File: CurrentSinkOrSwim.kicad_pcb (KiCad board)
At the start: 2 copper layers, 41.7 x 47.8 mm, 23 parts, among them P1 CONN_01X01, P101 CONN_01X02, P102 CONN_01X03, P103 CONN_01X02, Q401 BUK9575, U201 LMV358, U301 LM2931D-R

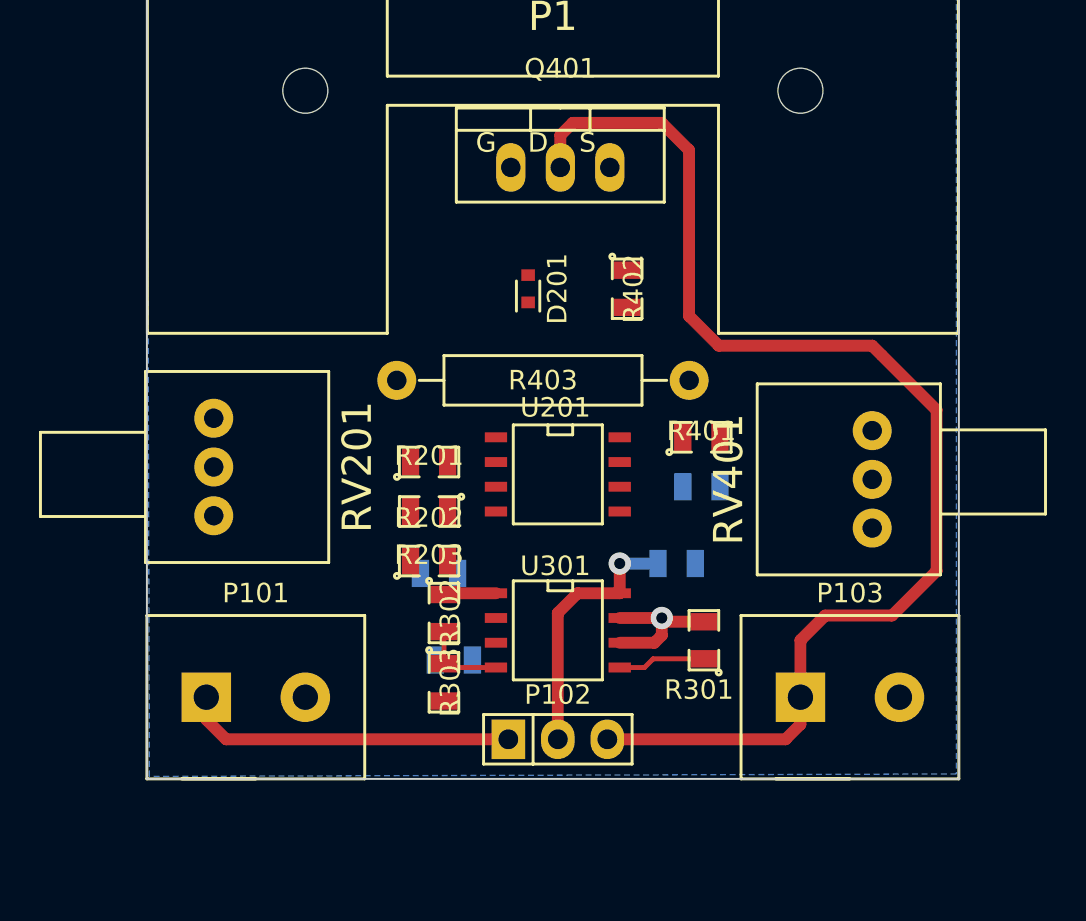
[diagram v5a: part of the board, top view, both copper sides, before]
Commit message: Moved pots/terms and routed traces to all components
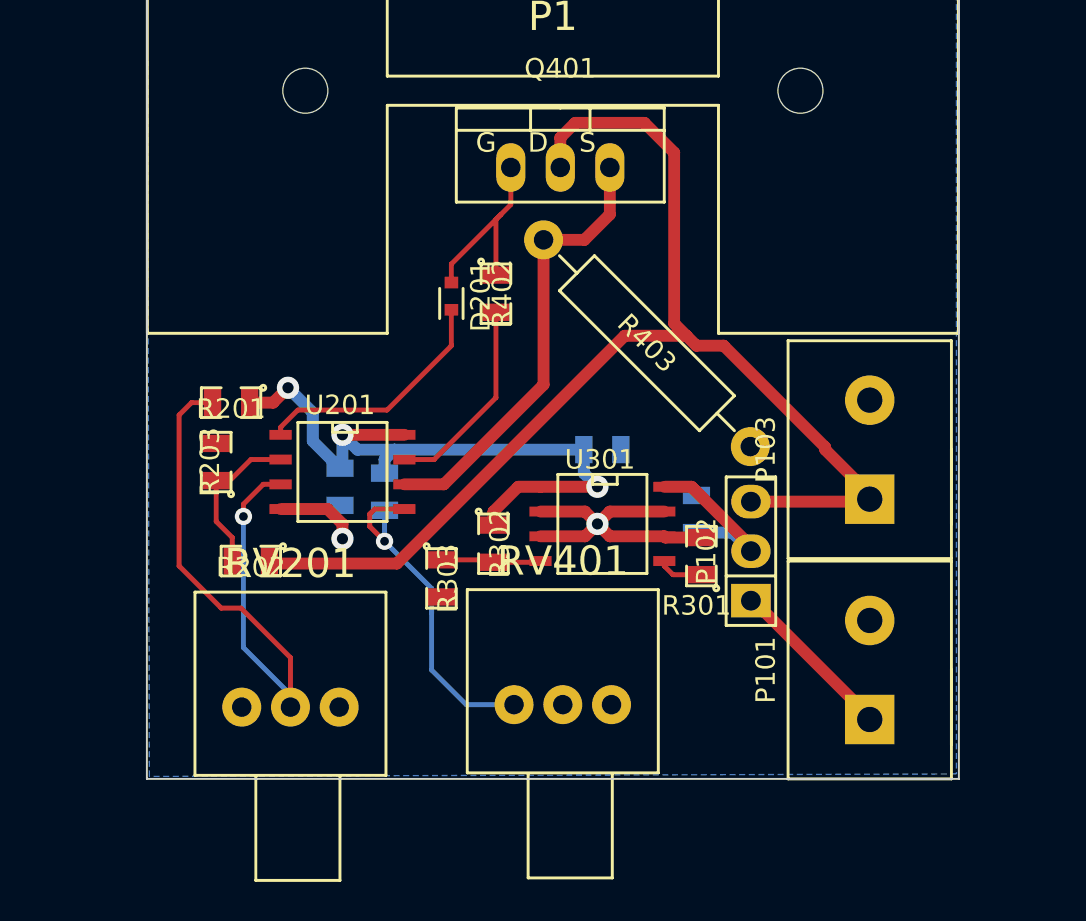
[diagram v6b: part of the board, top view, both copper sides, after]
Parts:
- removed C401: C, SMD_Packages:SMD-0805
- R401: moved to B.Cu
- moved P101 31.5 mm to (143.3, 78.0), turned to 90 degrees
- moved RV401 19.6 mm to (127.5, 79.8), turned to 0 degrees
- moved R401 16.5 mm to (118.4, 68.8), turned to 270 degrees
- moved P102 13.8 mm to (137.2, 71.9), turned to 90 degrees
- moved RV201 12.9 mm to (113.5, 79.9), turned to 0 degrees
- moved P103 12.7 mm to (143.3, 66.7), turned to 90 degrees
- moved R203 12.0 mm to (109.7, 67.3), turned to 90 degrees
- moved U201 11.0 mm to (116.2, 67.8)
- moved C201 10.6 mm to (116.1, 68.6), turned to 270 degrees
- moved R201 10.6 mm to (110.5, 64.3), turned to 180 degrees
- moved C302 10.5 mm to (129.5, 66.7), turned to 0 degrees
- moved R202 9.49 mm to (111.5, 72.4)
- moved R402 6.74 mm to (124.1, 58.7)
- moved U301 5.92 mm to (129.5, 70.5)
- moved R403 5.66 mm to (131.8, 61.2), turned to 315 degrees
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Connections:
- R203 pad 2: /Voltage Control/Current_Sink- -> GND
- RV201 pad 3: /Voltage Control/Current_Sink- -> GND
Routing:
- net Net-(R201-Pad2): track 0.00 -> 33.7 mm, vias 0 -> 1
- net 2.7V: track 2.69 -> 35.3 mm, vias 0 -> 3
- net Net-(Q401-PadS): track 0.00 -> 23.0 mm
- net Net-(R401-Pad2): track 0.00 -> 17.9 mm, vias 0 -> 1
- net Net-(D201-Pad2): track 0.00 -> 12.7 mm
- net GND: track 7.60 -> 20.2 mm, vias 1 -> 2
- net Net-(R402-Pad2): track 0.00 -> 10.4 mm
- net /Current Control/FET_Gate: track 0.00 -> 10.4 mm
- net Net-(P101-Pad1): track 17.1 -> 8.70 mm
- net Net-(R202-Pad2): track 0.00 -> 8.31 mm
- net /Power Regulation/Vin: track 13.6 -> 10.0 mm, vias 1 -> 0
- net Net-(R301-Pad1): track 4.50 -> 2.34 mm
- net Net-(R302-Pad2): track 4.40 -> 5.16 mm

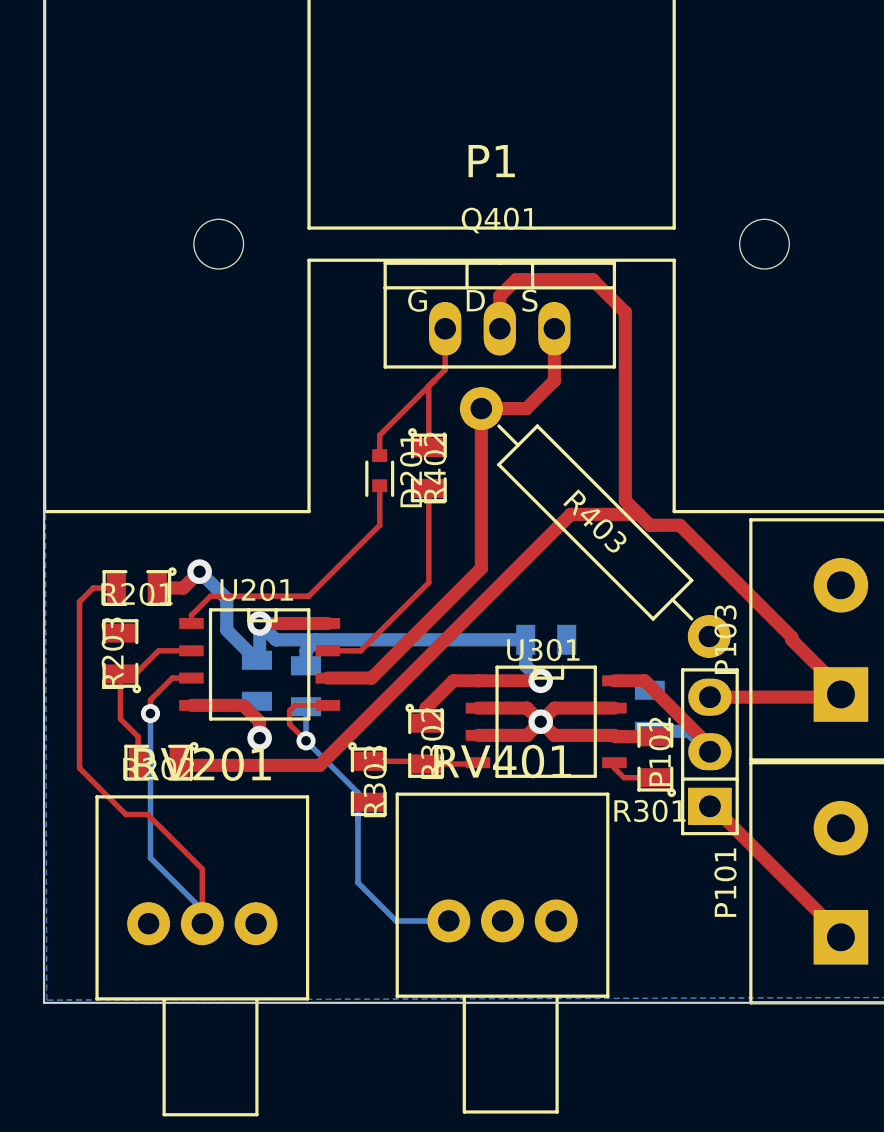
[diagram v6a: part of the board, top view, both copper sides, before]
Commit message: Ground fill and DRC
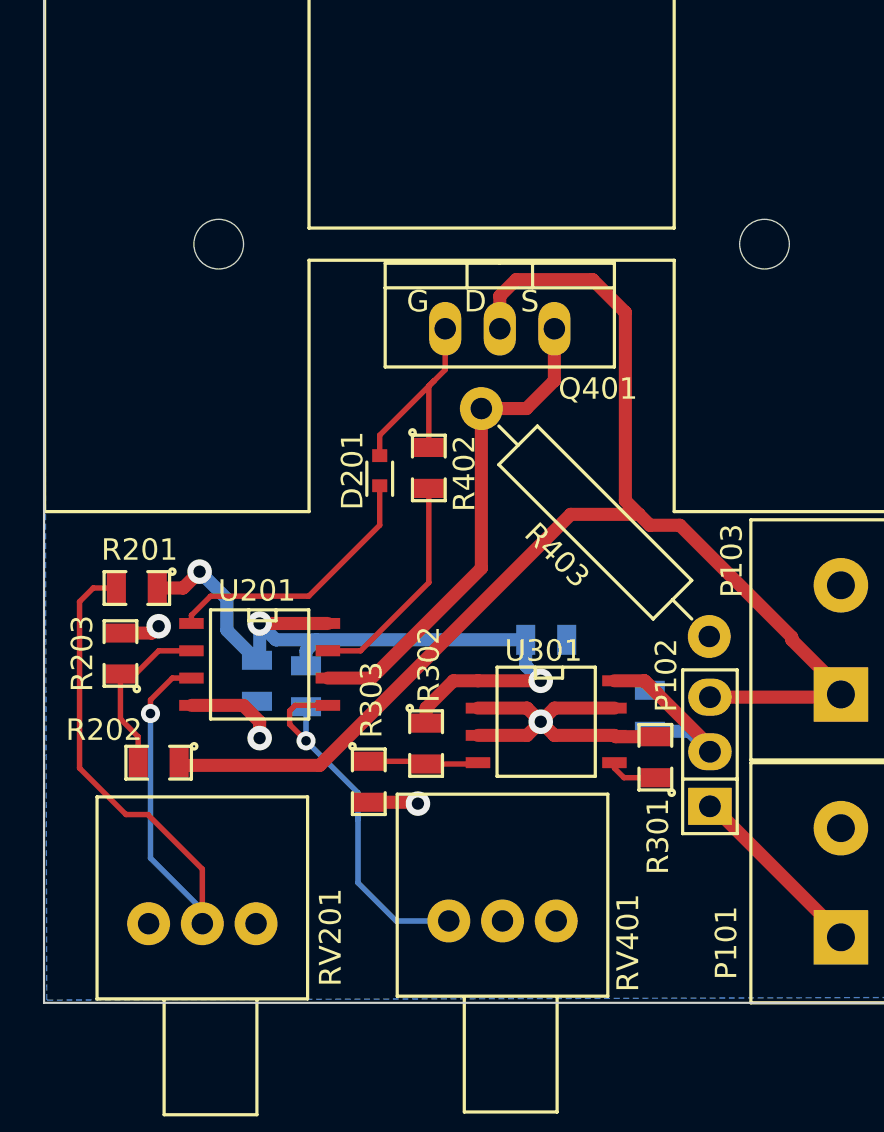
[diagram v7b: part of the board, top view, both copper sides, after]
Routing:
- net GND: track 20.2 -> 24.5 mm, vias 2 -> 4

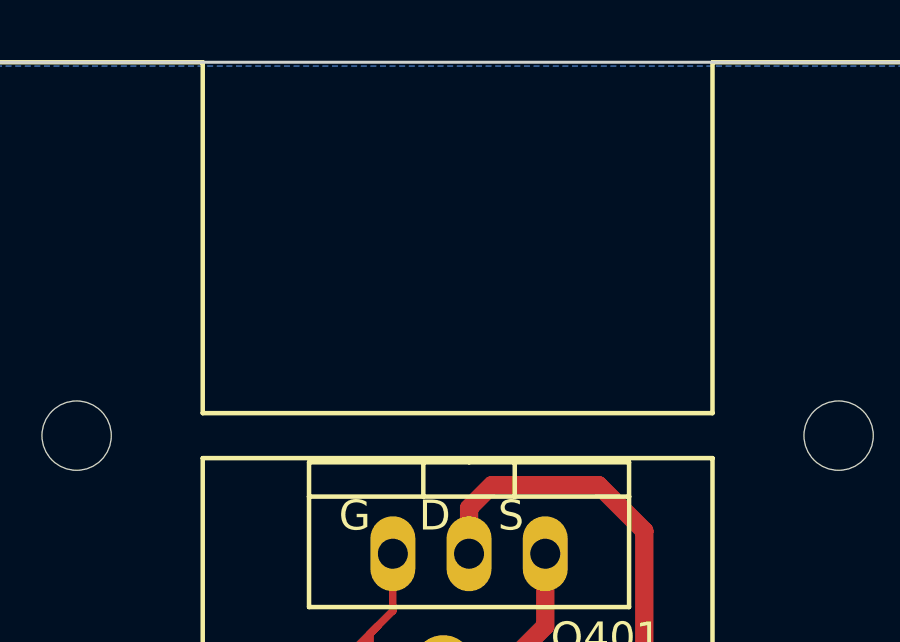
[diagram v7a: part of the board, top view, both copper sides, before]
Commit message: Added graphic and text above heatsink
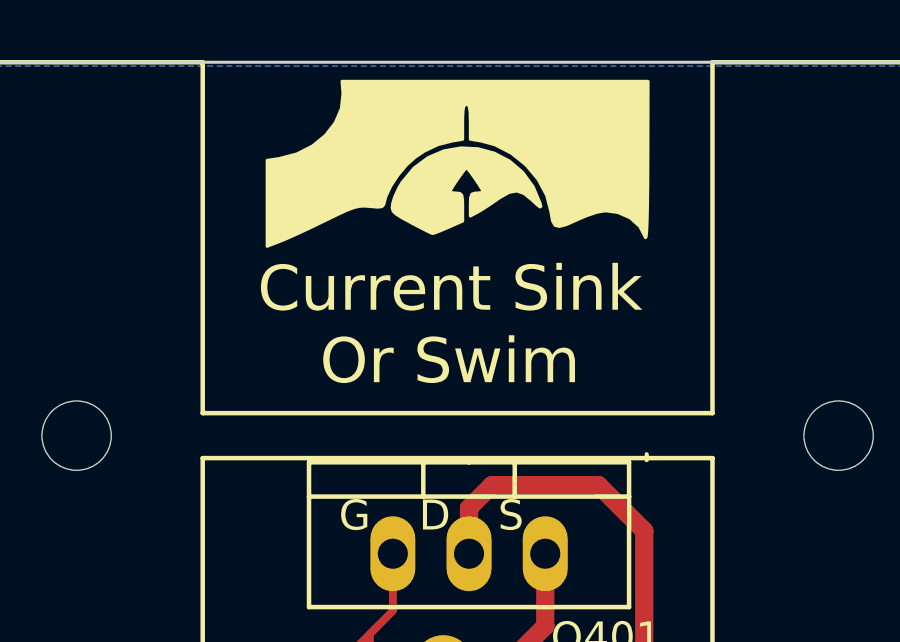
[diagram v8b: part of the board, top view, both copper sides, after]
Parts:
- added G***: LOGO, Current:CSOS, F.Cu at (127.0, 42.8)
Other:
- board text added: "Current Sink Or Swim"
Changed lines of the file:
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@@
 (kicad_pcb (version 4) (host pcbnew 0.201502010101+5397~21~ubuntu14.04.1-product)
   (general
-    (links 42)
+    (links 0)
     (no_connects 0)
-    (area 105.817599 35.434199 151.517134 89.152801)
+    (area 106.121999 35.763999 147.878001 83.616001)
     (thickness 1.6)
-    (drawings 4)
+    (drawings 5)
     (tracks 132)
     (zones 0)
-    (modules 22)
+    (modules 23)
     (nets 17)
   )
@@
     (34 B.Paste user)
     (35 F.Paste user)
-    (36 B.SilkS user hide)
+    (36 B.SilkS user)
     (37 F.SilkS user)
-    (38 B.Mask user hide)
+    (38 B.Mask user)
     (39 F.Mask user)
-    (40 Dwgs.User user hide)
+    (40 Dwgs.User user)
     (41 Cmts.User user)
-    (42 Eco1.User user hide)
-    (43 Eco2.User user hide)
+    (42 Eco1.User user)
+    (43 Eco2.User user)
     (44 Edge.Cuts user)
     (45 Margin user)
@@
     (pad_to_mask_clearance 0)
     (aux_axis_origin 0 0)
-    (visible_elements FFFF867F)
+    (visible_elements FFFFD7FF)
     (pcbplotparams
       (layerselection 0x00030_80000001)
@@
     (pad "" np_thru_hole oval (at -5.1 -3.3) (size 2 2.2) (drill oval 2 2.2) (layers *.Cu *.Mask F.SilkS))
   )
+  (module Current:CSOS (layer F.Cu)
+    (at 127 42.799)
+    (fp_text reference G*** (at 0 0) (layer F.SilkS) hide
+      (effects (font (thickness 0.3)))
+    )
+    (fp_text value LOGO (at 0.75 0) (layer F.SilkS) hide
+      (effects (font (thickness 0.3)))
+    )
+    (fp_poly (pts (xy 6.332589 6.248175) (xy 6.321406 6.2865) (xy 6.290503 6.297136) (xy 6.278701 6.180666)
+      (xy 6.292007 6.060471) (xy 6.321406 6.074833) (xy 6.332589 6.248175) (xy 6.332589 6.248175)) (layer F.SilkS) (width 0.1))
+    (fp_poly (pts (xy 6.35 -6.35) (xy 6.342364 -3.6195) (xy 6.338041 -2.844779) (xy 6.32992 -2.205589)
+      (xy 6.318217 -1.708474) (xy 6.30315 -1.359975) (xy 6.284937 -1.166635) (xy 6.263794 -1.134996)
+      (xy 6.260074 -1.14565) (xy 6.070103 -1.511787) (xy 5.754746 -1.796131) (xy 5.347069 -1.97661)
+      (xy 4.932164 -2.032) (xy 4.658011 -1.988116) (xy 4.293298 -1.867165) (xy 3.987667 -1.733968)
+      (xy 3.631328 -1.575223) (xy 3.393129 -1.511035) (xy 3.245805 -1.549173) (xy 3.162094 -1.697404)
+      (xy 3.114734 -1.963497) (xy 3.112456 -1.983355) (xy 2.968407 -2.545754) (xy 2.682376 -3.079807)
+      (xy 2.28171 -3.557623) (xy 1.79376 -3.95131) (xy 1.245874 -4.232976) (xy 0.783166 -4.358849)
+      (xy 0.423333 -4.417551) (xy 0.423333 -5.002776) (xy 0.415702 -5.322469) (xy 0.388292 -5.504557)
+      (xy 0.334326 -5.580271) (xy 0.296333 -5.588) (xy 0.226956 -5.552838) (xy 0.187441 -5.426531)
+      (xy 0.17101 -5.177851) (xy 0.169333 -5.002776) (xy 0.169333 -4.417551) (xy -0.181877 -4.358215)
+      (xy -0.66885 -4.233561) (xy -1.117966 -4.016975) (xy -1.41718 -3.817206) (xy -1.70709 -3.556147)
+      (xy -1.990765 -3.216269) (xy -2.230436 -2.850985) (xy -2.388332 -2.51371) (xy -2.420075 -2.398898)
+      (xy -2.458164 -2.244349) (xy -2.523351 -2.169874) (xy -2.662911 -2.154507) (xy -2.920638 -2.176926)
+      (xy -3.110434 -2.190699) (xy -3.279871 -2.181082) (xy -3.463619 -2.137161) (xy -3.696349 -2.048025)
+      (xy -4.01273 -1.90276) (xy -4.414301 -1.706803) (xy -4.843446 -1.498766) (xy -5.261431 -1.302511)
+      (xy -5.6233 -1.138746) (xy -5.884097 -1.028183) (xy -5.9055 -1.019844) (xy -6.35 -0.849138)
+      (xy -6.35 -2.282048) (xy -6.35 -3.714958) (xy -5.947834 -3.77494) (xy -5.360352 -3.928988)
+      (xy -4.839039 -4.193979) (xy -4.404201 -4.548819) (xy -4.076142 -4.972412) (xy -3.875168 -5.443665)
+      (xy -3.821583 -5.941482) (xy -3.824215 -5.981109) (xy -3.853554 -6.35) (xy 1.248223 -6.35)
+      (xy 6.35 -6.35) (xy 6.35 -6.35)) (layer F.SilkS) (width 0.1))
+    (fp_poly (pts (xy 2.775091 -2.176038) (xy 2.742605 -2.16183) (xy 2.630231 -2.252313) (xy 2.482437 -2.391834)
+      (xy 2.21545 -2.607974) (xy 1.974172 -2.69267) (xy 1.717188 -2.646432) (xy 1.40308 -2.469766)
+      (xy 1.312062 -2.406203) (xy 1.041096 -2.21941) (xy 0.78807 -2.057083) (xy 0.656166 -1.980695)
+      (xy 0.423333 -1.858319) (xy 0.423333 -2.241493) (xy 0.43199 -2.477447) (xy 0.47463 -2.589566)
+      (xy 0.576255 -2.623109) (xy 0.635 -2.624667) (xy 0.794269 -2.641222) (xy 0.846666 -2.672912)
+      (xy 0.802955 -2.764636) (xy 0.694539 -2.937779) (xy 0.555494 -3.142902) (xy 0.419898 -3.330567)
+      (xy 0.321828 -3.451336) (xy 0.296333 -3.471334) (xy 0.23311 -3.407918) (xy 0.113766 -3.250628)
+      (xy -0.02762 -3.048903) (xy -0.156974 -2.852181) (xy -0.240217 -2.7099) (xy -0.254 -2.672912)
+      (xy -0.181368 -2.63661) (xy -0.042334 -2.624667) (xy 0.078788 -2.612616) (xy 0.141917 -2.548868)
+      (xy 0.165826 -2.392029) (xy 0.169333 -2.157933) (xy 0.169333 -1.691199) (xy -0.306869 -1.4806)
+      (xy -0.565549 -1.370487) (xy -0.758831 -1.296161) (xy -0.836036 -1.275016) (xy -0.92966 -1.314833)
+      (xy -1.134919 -1.41701) (xy -1.414766 -1.562867) (xy -1.549709 -1.634849) (xy -1.864404 -1.806722)
+      (xy -2.056537 -1.927468) (xy -2.15326 -2.025087) (xy -2.18172 -2.127575) (xy -2.169067 -2.262932)
+      (xy -2.16768 -2.272141) (xy -2.096935 -2.50413) (xy -1.961875 -2.792888) (xy -1.858991 -2.969062)
+      (xy -1.45672 -3.456743) (xy -0.978768 -3.810553) (xy -0.448509 -4.033954) (xy 0.110679 -4.130411)
+      (xy 0.67542 -4.103388) (xy 1.222338 -3.95635) (xy 1.728057 -3.692761) (xy 2.1692 -3.316084)
+      (xy 2.522392 -2.829784) (xy 2.75031 -2.286) (xy 2.775091 -2.176038) (xy 2.775091 -2.176038)) (layer F.SilkS) (width 0.1))
+  )
+  (gr_text "Current Sink\nOr Swim" (at 126.746 44.577) (layer F.SilkS)
+    (effects (font (size 1.5 1.5) (thickness 0.3)))
+  )
   (gr_line (start 147.828 35.814) (end 106.172 35.814) (angle 90) (layer Edge.Cuts) (width 0.1))
